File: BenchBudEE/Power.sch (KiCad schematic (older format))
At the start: 13 parts, among them P1 CONN_12X2, SW1 SWITCH_INV

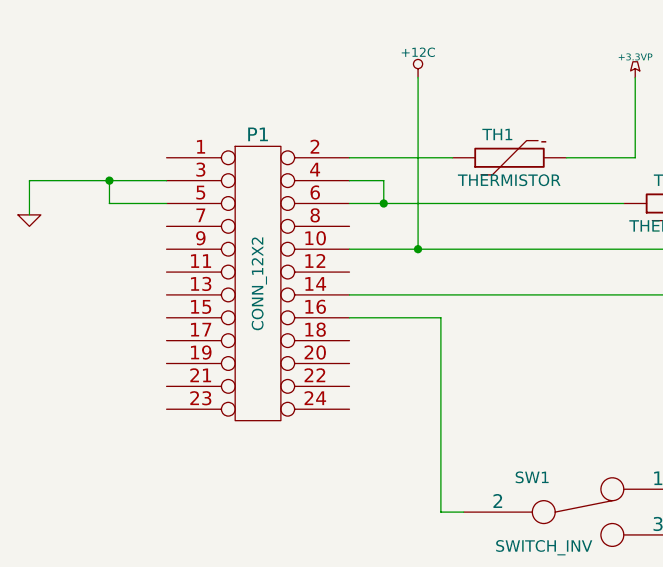
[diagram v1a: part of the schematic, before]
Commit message: Associating and Placing the Terminal Block Module
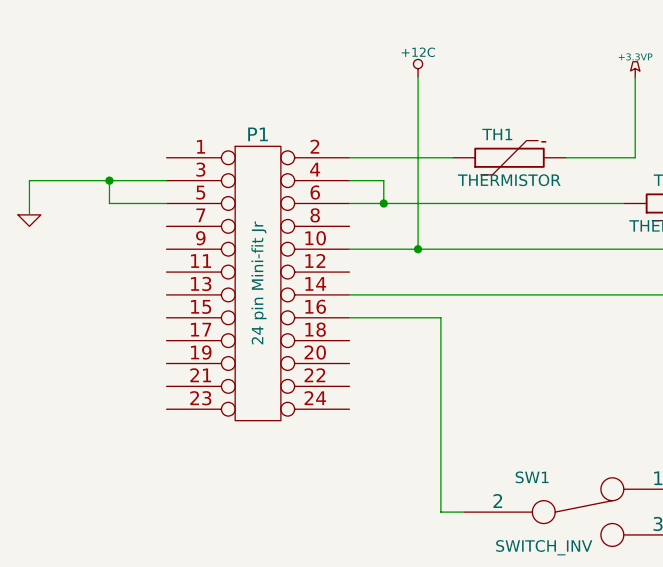
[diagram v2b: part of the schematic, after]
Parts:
- P1: value CONN_12X2 -> 24 pin Mini-fit Jr; MFG Name (none) -> MOLEX; MFG Part Number (none) -> 39-30-1240
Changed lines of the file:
@@
 Sheet 4 9
 Title ""
-Date "19 feb 2014"
+Date "22 feb 2014"
 Rev ""
 Comp ""
@@
 P 2700 1900
 F 0 "P1" H 2700 2550 60  0000 C CNN
-F 1 "CONN_12X2" V 2700 1900 50  0000 C CNN
+F 1 "24 pin Mini-fit Jr" V 2700 1900 50  0000 C CNN
 F 2 "" H 2700 1900 60  0000 C CNN
 F 3 "" H 2700 1900 60  0000 C CNN
+F 4 "MOLEX" H 2700 1900 60  0001 C CNN "MFG Name"
+F 5 "39-30-1240" H 2700 1900 60  0001 C CNN "MFG Part Number"
 	1    2700 1900
 	1    0    0    -1

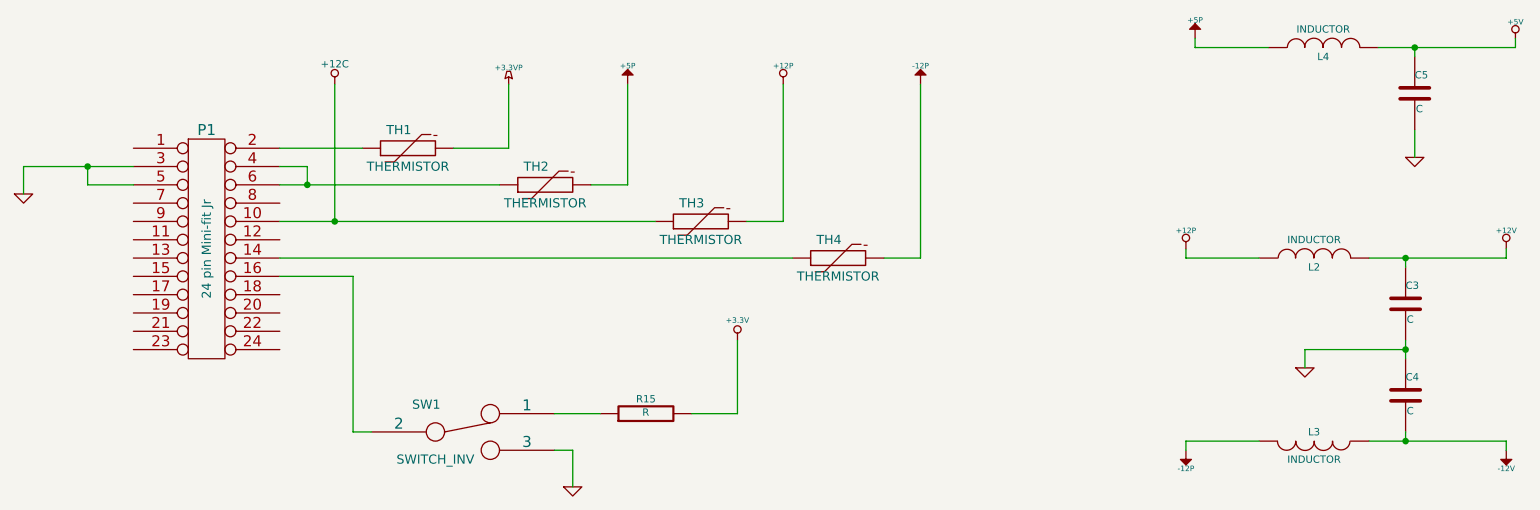
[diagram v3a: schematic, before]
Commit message: Associating and Placing the Power protection module
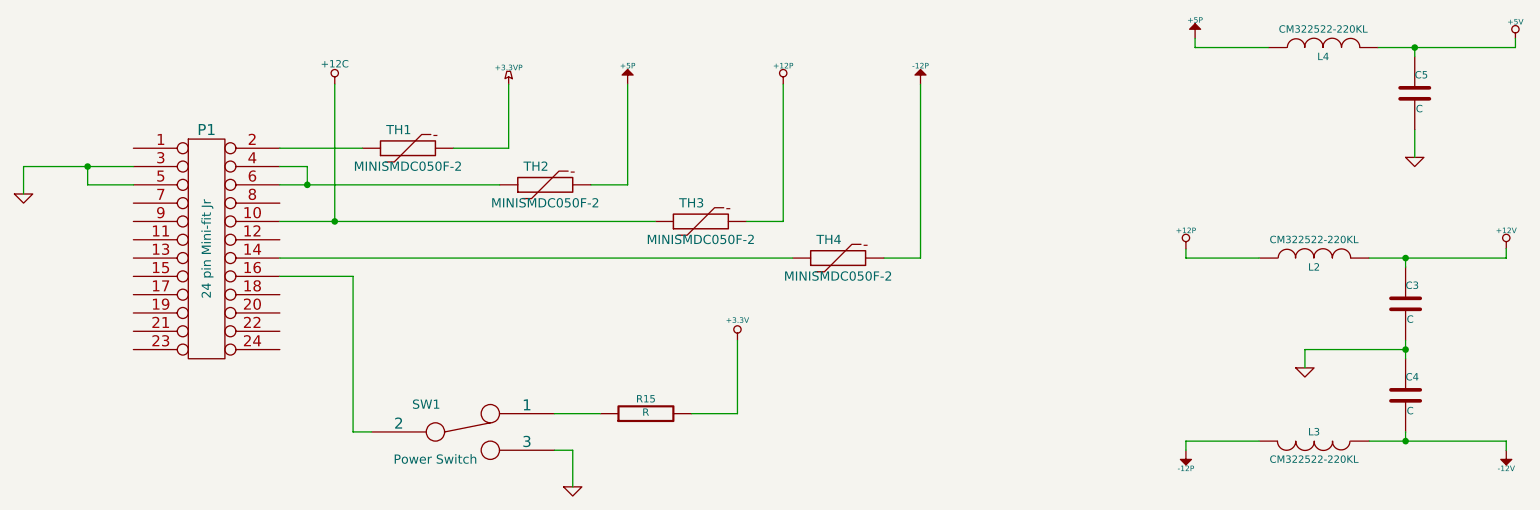
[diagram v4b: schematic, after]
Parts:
- L2, L3, L4: value INDUCTOR -> CM322522-220KL; MFG Name (none) -> Bournes; MFG Part Number (none) -> CM322522-220KL
- SW1: value SWITCH_INV -> Power Switch; MFG Name (none) -> C&K Components; MFG Part Number (none) -> OS102011MA1QN1
- TH1, TH2, TH3, TH4: value THERMISTOR -> MINISMDC050F-2; MFG Name (none) -> TE Connectivity; MFG Part Number (none) -> MINISMDC050F-2
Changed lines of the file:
@@
 Sheet 4 9
 Title ""
-Date "22 feb 2014"
+Date "23 feb 2014"
 Rev ""
 Comp ""
@@
 	1700 1450 1700 1600
 $Comp
-L GND #PWR23
+L GND #PWR023
 U 1 1 52F65191
 P 1700 1600
-F 0 "#PWR23" H 1700 1600 30  0001 C CNN
+F 0 "#PWR023" H 1700 1600 30  0001 C CNN
 F 1 "GND" H 1700 1530 30  0001 C CNN
 F 2 "" H 1700 1600 60  0000 C CNN
@@
 	3100 1950 5900 1950
 $Comp
-L +12P #PWR29
+L +12P #PWR024
 U 1 1 52F65291
 P 5850 1000
-F 0 "#PWR29" H 5850 970 30  0001 C CNN
+F 0 "#PWR024" H 5850 970 30  0001 C CNN
 F 1 "+12P" H 5850 1100 30  0000 C CNN
 F 2 "" H 5850 1000 60  0000 C CNN
@@
 	5850 1750 5650 1750
 $Comp
-L -12P #PWR30
+L -12P #PWR025
 U 1 1 52F65D56
 P 6600 1000
-F 0 "#PWR30" H 6600 1130 20  0001 C CNN
+F 0 "#PWR025" H 6600 1130 20  0001 C CNN
 F 1 "-12P" H 6600 1100 30  0000 C CNN
 F 2 "" H 6600 1000 60  0000 C CNN
@@
 P 4100 2900
 F 0 "SW1" H 3900 3050 50  0000 C CNN
-F 1 "SWITCH_INV" H 3950 2750 50  0000 C CNN
+F 1 "Power Switch" H 3950 2750 50  0000 C CNN
 F 2 "~" H 4100 2900 60  0000 C CNN
 F 3 "~" H 4100 2900 60  0000 C CNN
+F 4 "C&K Components" H 4100 2900 60  0001 C CNN "MFG Name"
+F 5 "OS102011MA1QN1" H 4100 2900 60  0001 C CNN "MFG Part Number"
 	1    4100 2900
 	1    0    0    -1
 $EndComp
 $Comp
-L GND #PWR26
+L GND #PWR026
 U 1 1 52F65E0B
 P 4700 3200
-F 0 "#PWR26" H 4700 3200 30  0001 C CNN
+F 0 "#PWR026" H 4700 3200 30  0001 C CNN
 F 1 "GND" H 4700 3130 30  0001 C CNN
 F 2 "" H 4700 3200 60  0000 C CNN
@@
 	5600 2800 5600 2400
 $Comp
-L +3.3V #PWR28
+L +3.3V #PWR027
 U 1 1 52F66046
 P 5600 2400
-F 0 "#PWR28" H 5600 2360 30  0001 C CNN
+F 0 "#PWR027" H 5600 2360 30  0001 C CNN
 F 1 "+3.3V" H 5600 2510 30  0000 C CNN
 F 2 "" H 5600 2400 60  0000 C CNN
@@
 $EndComp
 $Comp
-L -12P #PWR32
+L -12P #PWR028
 U 1 1 52F6604C
 P 8050 3000
-F 0 "#PWR32" H 8050 3130 20  0001 C CNN
+F 0 "#PWR028" H 8050 3130 20  0001 C CNN
 F 1 "-12P" H 8050 3100 30  0000 C CNN
 F 2 "" H 8050 3000 60  0000 C CNN
@@
 $EndComp
 $Comp
-L +12P #PWR31
+L +12P #PWR029
 U 1 1 52F66052
 P 8050 1900
-F 0 "#PWR31" H 8050 1870 30  0001 C CNN
+F 0 "#PWR029" H 8050 1870 30  0001 C CNN
 F 1 "+12P" H 8050 2000 30  0000 C CNN
 F 2 "" H 8050 1900 60  0000 C CNN
@@
 	1    8050 1900
 	1    0    0    -1
-$EndComp
-$Comp
-L INDUCTOR L2
-U 1 1 52F6605A
-P 8750 1950
-F 0 "L2" V 8700 1950 40  0000 C CNN
-F 1 "INDUCTOR" V 8850 1950 40  0000 C CNN
-F 2 "~" H 8750 1950 60  0000 C CNN
-F 3 "~" H 8750 1950 60  0000 C CNN
-	1    8750 1950
-	0    -1   -1   0
-$EndComp
-$Comp
-L INDUCTOR L3
-U 1 1 52F66067
-P 8750 2950
-F 0 "L3" V 8700 2950 40  0000 C CNN
-F 1 "INDUCTOR" V 8850 2950 40  0000 C CNN
-F 2 "~" H 8750 2950 60  0000 C CNN
-F 3 "~" H 8750 2950 60  0000 C CNN
-	1    8750 2950
-	0    1    1    0
 $EndComp
 $Comp
@@
 Connection ~ 9250 2450
 $Comp
-L GND #PWR34
+L GND #PWR030
 U 1 1 52F6614F
 P 8700 2550
-F 0 "#PWR34" H 8700 2550 30  0001 C CNN
+F 0 "#PWR030" H 8700 2550 30  0001 C CNN
 F 1 "GND" H 8700 2480 30  0001 C CNN
 F 2 "" H 8700 2550 60  0000 C CNN
@@
 Connection ~ 9250 1950
 $Comp
-L +12V #PWR36
+L +12V #PWR031
 U 1 1 52F661D8
 P 9800 1900
-F 0 "#PWR36" H 9800 1850 20  0001 C CNN
+F 0 "#PWR031" H 9800 1850 20  0001 C CNN
 F 1 "+12V" H 9800 2000 30  0000 C CNN
 F 2 "" H 9800 1900 60  0000 C CNN
@@
 $EndComp
 $Comp
-L -12V #PWR37
+L -12V #PWR032
 U 1 1 52F661F1
 P 9800 3000
-F 0 "#PWR37" H 9800 3130 20  0001 C CNN
+F 0 "#PWR032" H 9800 3130 20  0001 C CNN
 F 1 "-12V" H 9800 3100 30  0000 C CNN
 F 2 "" H 9800 3000 60  0000 C CNN
@@
 Connection ~ 3400 1750
 $Comp
-L +12C #PWR24
+L +12C #PWR033
 U 1 1 52FA733D
 P 3400 1000
-F 0 "#PWR24" H 3400 970 30  0001 C CNN
+F 0 "#PWR033" H 3400 970 30  0001 C CNN
 F 1 "+12C" H 3400 1110 40  0000 C CNN
 F 2 "" H 3400 1000 60  0000 C CNN
@@
 P 3800 1350
 F 0 "TH1" V 3900 1400 50  0000 C CNN
-F 1 "THERMISTOR" V 3700 1350 50  0000 C CNN
+F 1 "MINISMDC050F-2" V 3700 1350 50  0000 C CNN
 F 2 "~" H 3800 1350 60  0000 C CNN
 F 3 "~" H 3800 1350 60  0000 C CNN
+F 4 "TE Connectivity" H 3800 1350 60  0001 C CNN "MFG Name"
+F 5 "MINISMDC050F-2" H 3800 1350 60  0001 C CNN "MFG Part Number"
 	1    3800 1350
-	0    -1   -1   0
-$EndComp
-$Comp
-L THERMISTOR TH2
-U 1 1 52FA7AD9
-P 4550 1550
-F 0 "TH2" V 4650 1600 50  0000 C CNN
-F 1 "THERMISTOR" V 4450 1550 50  0000 C CNN
-F 2 "~" H 4550 1550 60  0000 C CNN
-F 3 "~" H 4550 1550 60  0000 C CNN
-	1    4550 1550
-	0    -1   -1   0
-$EndComp
-$Comp
-L THERMISTOR TH3
-U 1 1 52FA7ADF
-P 5400 1750
-F 0 "TH3" V 5500 1800 50  0000 C CNN
-F 1 "THERMISTOR" V 5300 1750 50  0000 C CNN
-F 2 "~" H 5400 1750 60  0000 C CNN
-F 3 "~" H 5400 1750 60  0000 C CNN
-	1    5400 1750
-	0    -1   -1   0
-$EndComp
-$Comp
-L THERMISTOR TH4
-U 1 1 52FA7AE5
-P 6150 1950
-F 0 "TH4" V 6250 2000 50  0000 C CNN
-F 1 "THERMISTOR" V 6050 1950 50  0000 C CNN
-F 2 "~" H 6150 1950 60  0000 C CNN
-F 3 "~" H 6150 1950 60  0000 C CNN
-	1    6150 1950
 	0    -1   -1   0
 $EndComp
@@
 P 8800 800
 F 0 "L4" V 8750 800 40  0000 C CNN
-F 1 "INDUCTOR" V 8900 800 40  0000 C CNN
+F 1 "CM322522-220KL" V 8900 800 40  0000 C CNN
 F 2 "~" H 8800 800 60  0000 C CNN
 F 3 "~" H 8800 800 60  0000 C CNN
+F 4 "Bournes" H 8800 800 60  0001 C CNN "MFG Name"
+F 5 "CM322522-220KL" H 8800 800 60  0001 C CNN "MFG Part Number"
 	1    8800 800
 	0    -1   -1   0
@@
 	9300 1250 9300 1400
 $Comp
-L GND #PWR35
+L GND #PWR034
 U 1 1 5300ADC6
 P 9300 1400
-F 0 "#PWR35" H 9300 1400 30  0001 C CNN
+F 0 "#PWR034" H 9300 1400 30  0001 C CNN
 F 1 "GND" H 9300 1330 30  0001 C CNN
 F 2 "" H 9300 1400 60  0000 C CNN
@@
 $EndComp
 $Comp
-L +3.3VP #PWR25
+L +3.3VP #PWR035
 U 1 1 5300AE54
 P 4350 1000
-F 0 "#PWR25" H 4400 1030 20  0001 C CNN
+F 0 "#PWR035" H 4400 1030 20  0001 C CNN
 F 1 "+3.3VP" H 4350 1090 30  0000 C CNN
 F 2 "" H 4350 1000 60  0000 C CNN
@@
 $EndComp
 $Comp
-L +5V #PWR38
+L +5V #PWR036
 U 1 1 5300AE69
 P 9850 750
-F 0 "#PWR38" H 9850 840 20  0001 C CNN
+F 0 "#PWR036" H 9850 840 20  0001 C CNN
 F 1 "+5V" H 9850 840 30  0000 C CNN
 F 2 "" H 9850 750 60  0000 C CNN
@@
 	1    0    0    -1
 $EndComp
+$Comp
+L THERMISTOR TH2
+U 1 1 5309D3C3
+P 4550 1550
+F 0 "TH2" V 4650 1600 50  0000 C CNN
+F 1 "MINISMDC050F-2" V 4450 1550 50  0000 C CNN
+F 2 "~" H 4550 1550 60  0000 C CNN
+F 3 "~" H 4550 1550 60  0000 C CNN
+F 4 "TE Connectivity" H 4550 1550 60  0001 C CNN "MFG Name"
+F 5 "MINISMDC050F-2" H 4550 1550 60  0001 C CNN "MFG Part Number"
+	1    4550 1550
+	0    -1   -1   0
+$EndComp
+$Comp
+L THERMISTOR TH3
+U 1 1 5309D3CB
+P 5400 1750
+F 0 "TH3" V 5500 1800 50  0000 C CNN
+F 1 "MINISMDC050F-2" V 5300 1750 50  0000 C CNN
+F 2 "~" H 5400 1750 60  0000 C CNN
+F 3 "~" H 5400 1750 60  0000 C CNN
+F 4 "TE Connectivity" H 5400 1750 60  0001 C CNN "MFG Name"
+F 5 "MINISMDC050F-2" H 5400 1750 60  0001 C CNN "MFG Part Number"
+	1    5400 1750
+	0    -1   -1   0
+$EndComp
+$Comp
+L THERMISTOR TH4
+U 1 1 5309D3E1
+P 6150 1950
+F 0 "TH4" V 6250 2000 50  0000 C CNN
+F 1 "MINISMDC050F-2" V 6050 1950 50  0000 C CNN
+F 2 "~" H 6150 1950 60  0000 C CNN
+F 3 "~" H 6150 1950 60  0000 C CNN
+F 4 "TE Connectivity" H 6150 1950 60  0001 C CNN "MFG Name"
+F 5 "MINISMDC050F-2" H 6150 1950 60  0001 C CNN "MFG Part Number"
+	1    6150 1950
+	0    -1   -1   0
+$EndComp
+$Comp
+L INDUCTOR L2
+U 1 1 5309D459
+P 8750 1950
+F 0 "L2" V 8700 1950 40  0000 C CNN
+F 1 "CM322522-220KL" V 8850 1950 40  0000 C CNN
+F 2 "~" H 8750 1950 60  0000 C CNN
+F 3 "~" H 8750 1950 60  0000 C CNN
+F 4 "Bournes" H 8750 1950 60  0001 C CNN "MFG Name"
+F 5 "CM322522-220KL" H 8750 1950 60  0001 C CNN "MFG Part Number"
+	1    8750 1950
+	0    -1   -1   0
+$EndComp
+$Comp
+L INDUCTOR L3
+U 1 1 5309D461
+P 8750 2950
+F 0 "L3" V 8700 2950 40  0000 C CNN
+F 1 "CM322522-220KL" V 8850 2950 40  0000 C CNN
+F 2 "~" H 8750 2950 60  0000 C CNN
+F 3 "~" H 8750 2950 60  0000 C CNN
+F 4 "Bournes" H 8750 2950 60  0001 C CNN "MFG Name"
+F 5 "CM322522-220KL" H 8750 2950 60  0001 C CNN "MFG Part Number"
+	1    8750 2950
+	0    1    1    0
+$EndComp
 $EndSCHEMATC

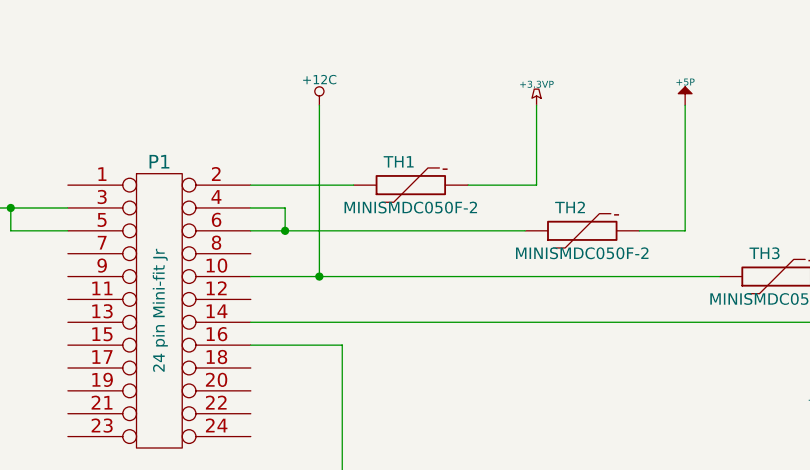
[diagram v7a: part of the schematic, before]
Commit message: Ground and Power Planes
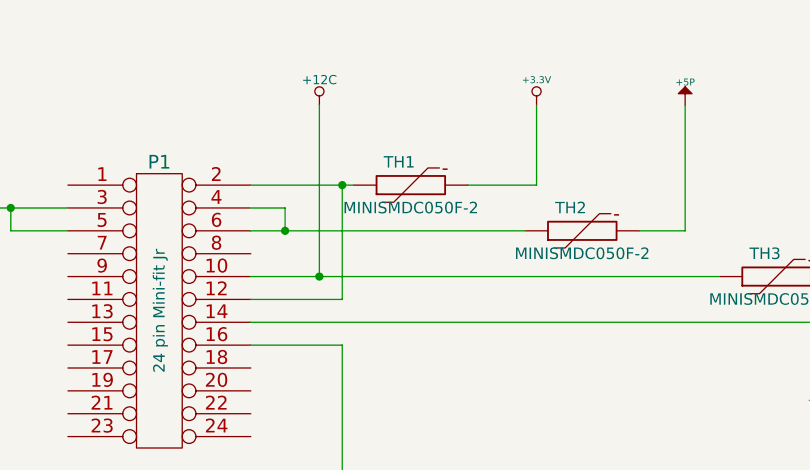
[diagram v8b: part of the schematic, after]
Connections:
- net +3.3VP is gone; now on net +3.3V: TH1.2
- net at P1.12 (P12): now also P1.2 (P2), TH1.1
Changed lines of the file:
@@
 Sheet 4 9
 Title ""
-Date "27 feb 2014"
+Date "1 mar 2014"
 Rev ""
 Comp ""
@@
 	1700 1450 1700 1600
 $Comp
-L GND #PWR022
+L GND #PWR22
 U 1 1 52F65191
 P 1700 1600
-F 0 "#PWR022" H 1700 1600 30  0001 C CNN
+F 0 "#PWR22" H 1700 1600 30  0001 C CNN
 F 1 "GND" H 1700 1530 30  0001 C CNN
 F 2 "" H 1700 1600 60  0000 C CNN
@@
 	3100 1950 5900 1950
 $Comp
-L +12P #PWR023
+L +12P #PWR28
 U 1 1 52F65291
 P 5850 1000
-F 0 "#PWR023" H 5850 970 30  0001 C CNN
+F 0 "#PWR28" H 5850 970 30  0001 C CNN
 F 1 "+12P" H 5850 1100 30  0000 C CNN
 F 2 "" H 5850 1000 60  0000 C CNN
@@
 	5850 1750 5650 1750
 $Comp
-L -12P #PWR024
+L -12P #PWR29
 U 1 1 52F65D56
 P 6600 1000
-F 0 "#PWR024" H 6600 1130 20  0001 C CNN
+F 0 "#PWR29" H 6600 1130 20  0001 C CNN
 F 1 "-12P" H 6600 1100 30  0000 C CNN
 F 2 "" H 6600 1000 60  0000 C CNN
@@
 $EndComp
 $Comp
-L GND #PWR025
+L GND #PWR25
 U 1 1 52F65E0B
 P 4700 3200
-F 0 "#PWR025" H 4700 3200 30  0001 C CNN
+F 0 "#PWR25" H 4700 3200 30  0001 C CNN
 F 1 "GND" H 4700 3130 30  0001 C CNN
 F 2 "" H 4700 3200 60  0000 C CNN
@@
 	5600 2800 5600 2400
 $Comp
-L +3.3V #PWR026
+L +3.3V #PWR27
 U 1 1 52F66046
 P 5600 2400
-F 0 "#PWR026" H 5600 2360 30  0001 C CNN
+F 0 "#PWR27" H 5600 2360 30  0001 C CNN
 F 1 "+3.3V" H 5600 2510 30  0000 C CNN
 F 2 "" H 5600 2400 60  0000 C CNN
@@
 $EndComp
 $Comp
-L -12P #PWR027
+L -12P #PWR31
 U 1 1 52F6604C
 P 8050 3000
-F 0 "#PWR027" H 8050 3130 20  0001 C CNN
+F 0 "#PWR31" H 8050 3130 20  0001 C CNN
 F 1 "-12P" H 8050 3100 30  0000 C CNN
 F 2 "" H 8050 3000 60  0000 C CNN
@@
 $EndComp
 $Comp
-L +12P #PWR028
+L +12P #PWR30
 U 1 1 52F66052
 P 8050 1900
-F 0 "#PWR028" H 8050 1870 30  0001 C CNN
+F 0 "#PWR30" H 8050 1870 30  0001 C CNN
 F 1 "+12P" H 8050 2000 30  0000 C CNN
 F 2 "" H 8050 1900 60  0000 C CNN
@@
 Connection ~ 9250 2450
 $Comp
-L GND #PWR029
+L GND #PWR33
 U 1 1 52F6614F
 P 8700 2550
-F 0 "#PWR029" H 8700 2550 30  0001 C CNN
+F 0 "#PWR33" H 8700 2550 30  0001 C CNN
 F 1 "GND" H 8700 2480 30  0001 C CNN
 F 2 "" H 8700 2550 60  0000 C CNN
@@
 Connection ~ 9250 1950
 $Comp
-L +12V #PWR030
+L +12V #PWR35
 U 1 1 52F661D8
 P 9800 1900
-F 0 "#PWR030" H 9800 1850 20  0001 C CNN
+F 0 "#PWR35" H 9800 1850 20  0001 C CNN
 F 1 "+12V" H 9800 2000 30  0000 C CNN
 F 2 "" H 9800 1900 60  0000 C CNN
@@
 $EndComp
 $Comp
-L -12V #PWR031
+L -12V #PWR36
 U 1 1 52F661F1
 P 9800 3000
-F 0 "#PWR031" H 9800 3130 20  0001 C CNN
+F 0 "#PWR36" H 9800 3130 20  0001 C CNN
 F 1 "-12V" H 9800 3100 30  0000 C CNN
 F 2 "" H 9800 3000 60  0000 C CNN
@@
 Connection ~ 3400 1750
 $Comp
-L +12C #PWR032
+L +12C #PWR23
 U 1 1 52FA733D
 P 3400 1000
-F 0 "#PWR032" H 3400 970 30  0001 C CNN
+F 0 "#PWR23" H 3400 970 30  0001 C CNN
 F 1 "+12C" H 3400 1110 40  0000 C CNN
 F 2 "" H 3400 1000 60  0000 C CNN
@@
 Wire Wire Line
 	9100 800  9850 800
-Wire Wire Line
-	9300 1300 9300 1300
-Wire Wire Line
-	9300 1250 9300 1400
-$Comp
-L GND #PWR033
+$Comp
+L GND #PWR34
 U 1 1 5300ADC6
 P 9300 1400
-F 0 "#PWR033" H 9300 1400 30  0001 C CNN
+F 0 "#PWR34" H 9300 1400 30  0001 C CNN
 F 1 "GND" H 9300 1330 30  0001 C CNN
 F 2 "" H 9300 1400 60  0000 C CNN
@@
 Connection ~ 9300 800
 $Comp
-L +5P #PWR27
+L +5P #PWR26
 U 1 1 5300AE45
 P 5000 1000
-F 0 "#PWR27" H 5000 1130 20  0001 C CNN
+F 0 "#PWR26" H 5000 1130 20  0001 C CNN
 F 1 "+5P" H 5000 1100 30  0000 C CNN
 F 2 "" H 5000 1000 60  0000 C CNN
@@
 $EndComp
 $Comp
-L +3.3VP #PWR034
-U 1 1 5300AE54
-P 4350 1000
-F 0 "#PWR034" H 4400 1030 20  0001 C CNN
-F 1 "+3.3VP" H 4350 1090 30  0000 C CNN
-F 2 "" H 4350 1000 60  0000 C CNN
-F 3 "" H 4350 1000 60  0000 C CNN
-	1    4350 1000
-	1    0    0    -1
-$EndComp
-$Comp
-L +5P #PWR33
+L +5P #PWR32
 U 1 1 5300AE61
 P 8100 750
-F 0 "#PWR33" H 8100 880 20  0001 C CNN
+F 0 "#PWR32" H 8100 880 20  0001 C CNN
 F 1 "+5P" H 8100 850 30  0000 C CNN
 F 2 "" H 8100 750 60  0000 C CNN
@@
 $EndComp
 $Comp
-L +5V #PWR035
+L +5V #PWR37
 U 1 1 5300AE69
 P 9850 750
-F 0 "#PWR035" H 9850 840 20  0001 C CNN
+F 0 "#PWR37" H 9850 840 20  0001 C CNN
 F 1 "+5V" H 9850 840 30  0000 C CNN
 F 2 "" H 9850 750 60  0000 C CNN
@@
 	0    1    1    0
 $EndComp
+Wire Wire Line
+	9300 1250 9300 1400
+$Comp
+L +3.3V #PWR24
+U 1 1 5311B0C2
+P 4350 1000
+F 0 "#PWR24" H 4350 960 30  0001 C CNN
+F 1 "+3.3V" H 4350 1110 30  0000 C CNN
+F 2 "" H 4350 1000 60  0000 C CNN
+F 3 "" H 4350 1000 60  0000 C CNN
+	1    4350 1000
+	1    0    0    -1
+$EndComp
+Wire Wire Line
+	3100 1850 3500 1850
+Wire Wire Line
+	3500 1850 3500 1350
+Connection ~ 3500 1350
 $EndSCHEMATC
